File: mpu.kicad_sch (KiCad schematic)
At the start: 15 parts, among them SW401 SW_DIP_x03, U401 STM32MP135FAE7

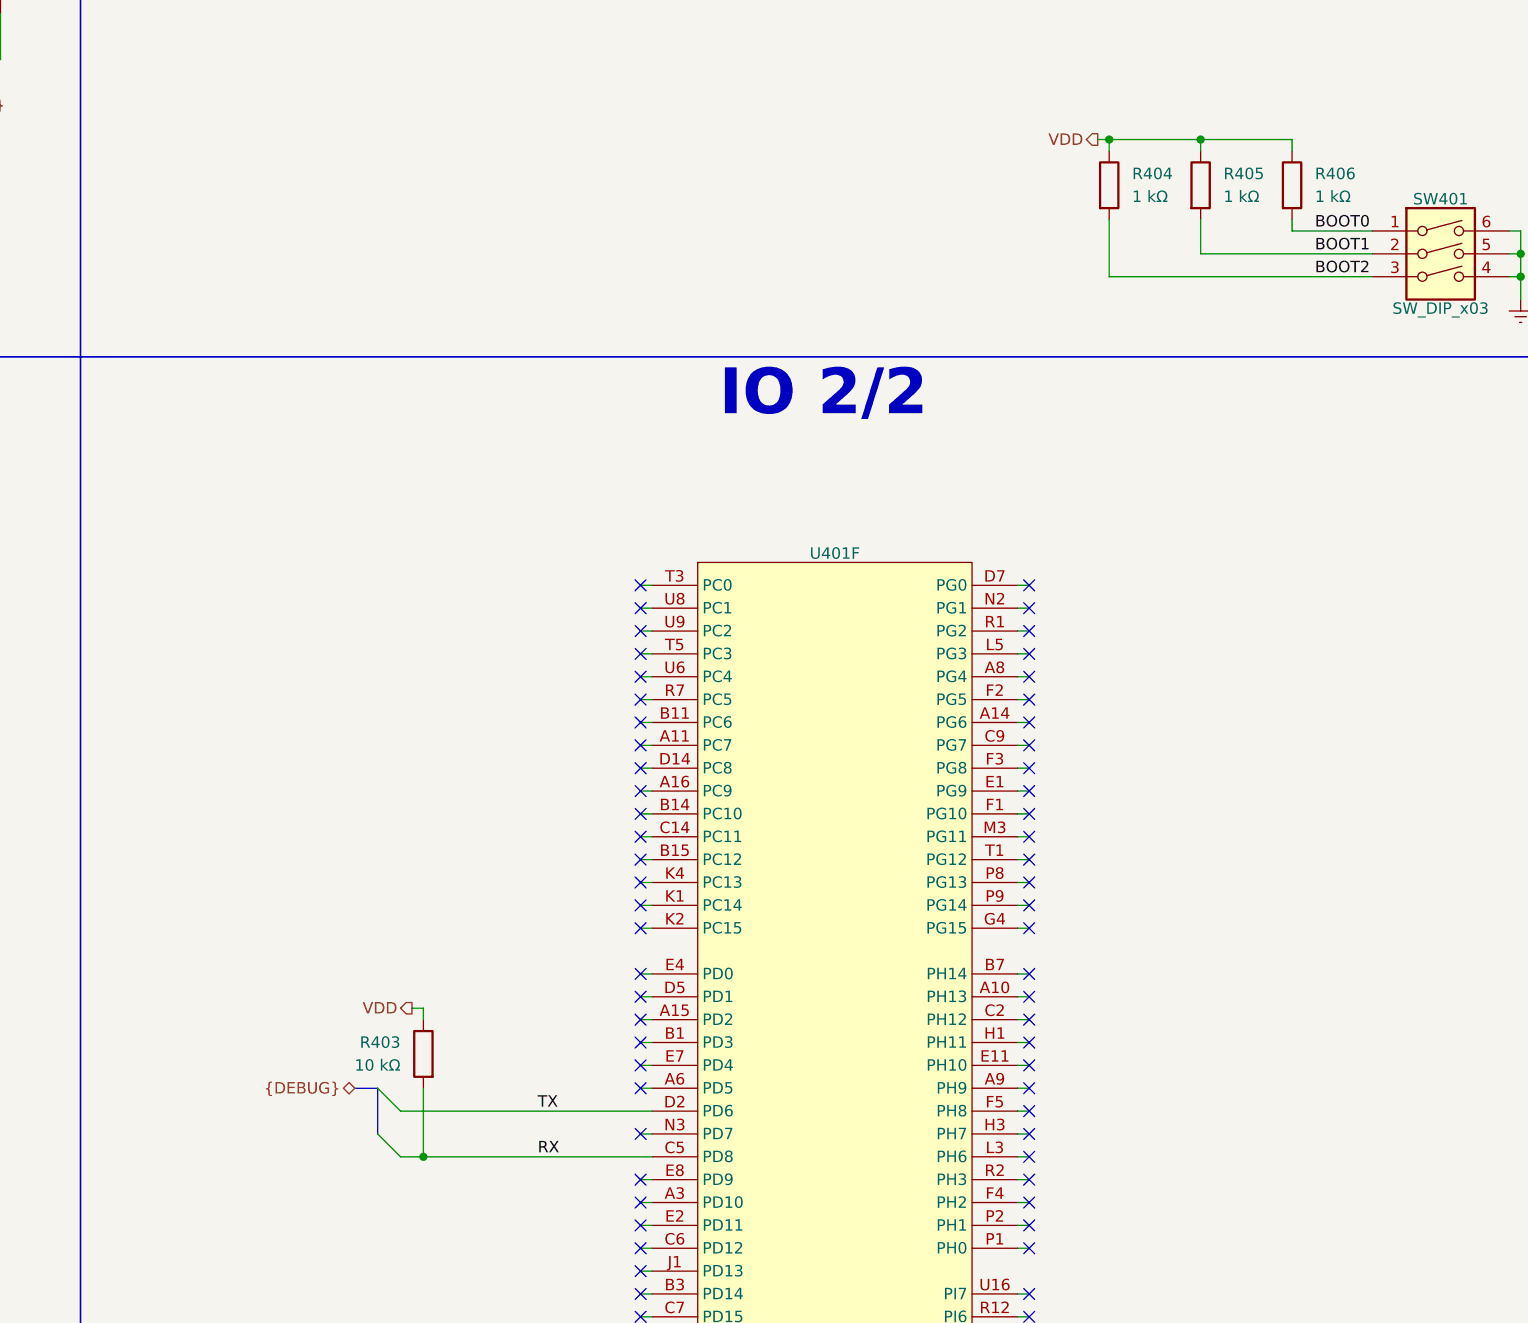
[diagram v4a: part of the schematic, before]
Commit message: Add 10k pull-ups to debug uart
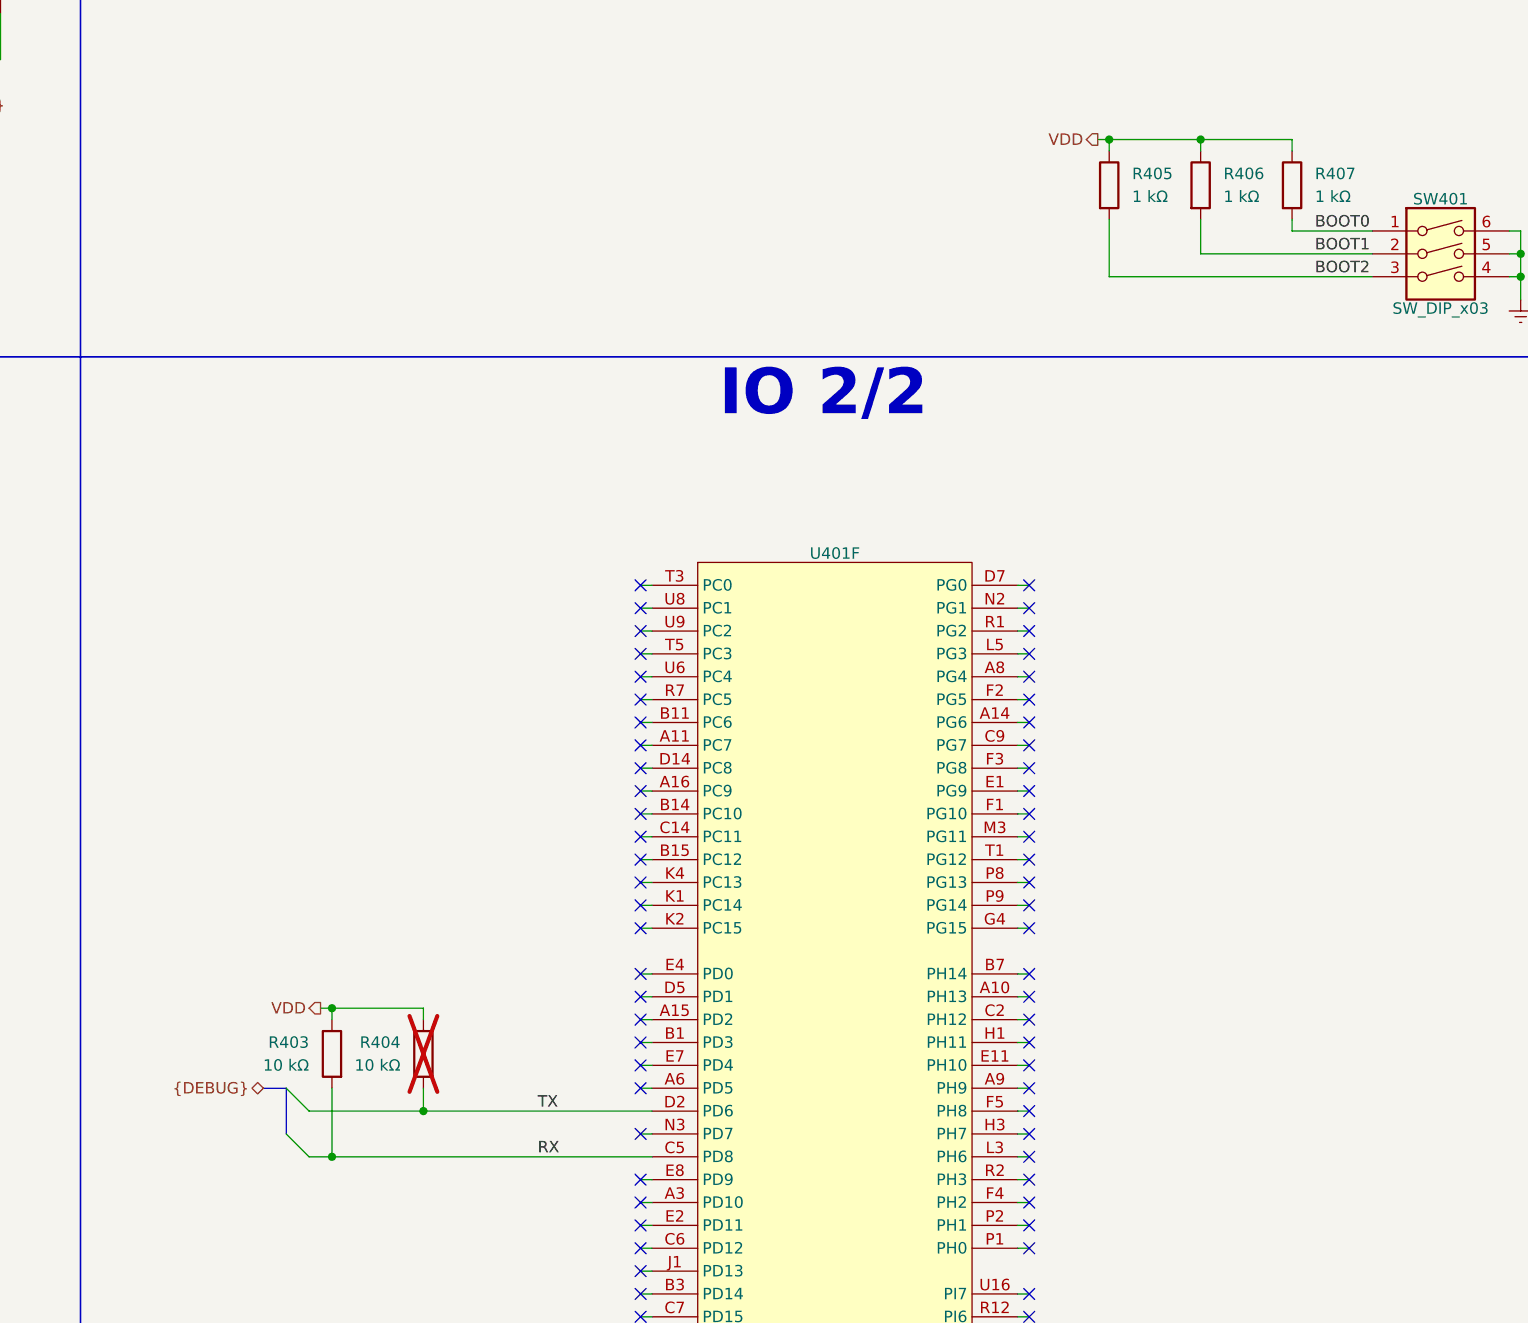
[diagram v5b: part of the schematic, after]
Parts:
- added R404: 10 kΩ, perfect_footprints:R_0402_1005Metric, symbol Device:R
- renumbered R404 to R405, R405 to R406, R406 to R407
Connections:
- net TX: now also R404.2
- net VDD: now also R404.1
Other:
- moved on the sheet: R403
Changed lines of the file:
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@@
 	)
 	(junction
+		(at 279.4 198.12)
+		(diameter 0)
+		(color 0 0 0 0)
+	)
+	(junction
 		(at 83.82 92.71)
 		(diameter 0)
@@
 	)
 	(junction
+		(at 269.24 186.69)
+		(diameter 0)
+		(color 0 0 0 0)
+	)
+	(junction
 		(at 102.87 228.6)
 		(diameter 0)
@@
 	)
 	(junction
-		(at 279.4 203.2)
+		(at 269.24 203.2)
 		(diameter 0)
 		(color 0 0 0 0)
@@
 	)
 	(bus_entry
-		(at 274.32 200.66)
+		(at 264.16 200.66)
 		(size 2.54 2.54)
 		(stroke
@@
 	)
 	(bus_entry
-		(at 274.32 195.58)
+		(at 264.16 195.58)
 		(size 2.54 2.54)
 		(stroke
@@
 	(wire
 		(pts
-			(xy 279.4 186.69) (xy 279.4 187.96)
+			(xy 269.24 186.69) (xy 269.24 187.96)
 		)
 		(stroke
@@
 	(bus
 		(pts
-			(xy 274.32 200.66) (xy 274.32 195.58)
+			(xy 264.16 200.66) (xy 264.16 195.58)
 		)
 		(stroke
@@
 		)
 	)
+	(wire
+		(pts
+			(xy 279.4 195.58) (xy 279.4 198.12)
+		)
+		(stroke
+			(width 0)
+			(type default)
+		)
+	)
 	(bus
 		(pts
@@
 	(wire
 		(pts
-			(xy 279.4 195.58) (xy 279.4 203.2)
+			(xy 269.24 195.58) (xy 269.24 203.2)
 		)
 		(stroke
@@
 	(wire
 		(pts
-			(xy 304.8 203.2) (xy 279.4 203.2)
+			(xy 304.8 203.2) (xy 269.24 203.2)
 		)
 		(stroke
@@
 	(wire
 		(pts
+			(xy 279.4 198.12) (xy 266.7 198.12)
+		)
+		(stroke
+			(width 0)
+			(type default)
+		)
+	)
+	(wire
+		(pts
 			(xy 87.63 154.94) (xy 100.33 154.94)
 		)
@@
 	(wire
 		(pts
-			(xy 279.4 203.2) (xy 276.86 203.2)
+			(xy 269.24 203.2) (xy 266.7 203.2)
 		)
 		(stroke
@@
 	(wire
 		(pts
+			(xy 279.4 187.96) (xy 279.4 186.69)
+		)
+		(stroke
+			(width 0)
+			(type default)
+		)
+	)
+	(wire
+		(pts
 			(xy 163.83 158.75) (xy 162.56 158.75)
 		)
@@
 	(bus
 		(pts
-			(xy 271.78 195.58) (xy 274.32 195.58)
+			(xy 261.62 195.58) (xy 264.16 195.58)
 		)
 		(stroke
@@
 	(wire
 		(pts
-			(xy 278.13 186.69) (xy 279.4 186.69)
+			(xy 267.97 186.69) (xy 269.24 186.69)
 		)
 		(stroke
@@
 		)
 	)
+	(wire
+		(pts
+			(xy 269.24 186.69) (xy 279.4 186.69)
+		)
+		(stroke
+			(width 0)
+			(type default)
+		)
+	)
 	(bus
 		(pts
@@
 	(wire
 		(pts
-			(xy 304.8 198.12) (xy 276.86 198.12)
+			(xy 304.8 198.12) (xy 279.4 198.12)
 		)
 		(stroke
@@
 	(hierarchical_label "{DEBUG}"
 		(shape bidirectional)
-		(at 271.78 195.58 180)
+		(at 261.62 195.58 180)
 		(effects
 			(font
@@
 	(hierarchical_label "VDD"
 		(shape output)
-		(at 278.13 186.69 180)
+		(at 267.97 186.69 180)
 		(effects
 			(font
@@
 		(in_bom yes)
 		(on_board yes)
-		(dnp no)
-		(property "Reference" "R403"
+		(dnp yes)
+		(property "Reference" "R404"
 			(at 276.86 190.4999 0)
 			(effects
@@
 			(project "linux-sbc"
 				(path "/fa11a02f-8043-4153-ab69-88d766503017/2d01087b-54dc-4f43-9cc7-a0ba17201776"
+					(reference "R404")
+					(unit 1)
+				)
+			)
+		)
+	)
+	(symbol
+		(lib_id "Device:R")
+		(at 269.24 191.77 0)
+		(mirror y)
+		(unit 1)
+		(exclude_from_sim no)
+		(in_bom yes)
+		(on_board yes)
+		(dnp no)
+		(property "Reference" "R403"
+			(at 266.7 190.4999 0)
+			(effects
+				(font
+					(size 1.27 1.27)
+				)
+				(justify left)
+			)
+		)
+		(property "Value" "10 kΩ"
+			(at 266.7 193.0399 0)
+			(effects
+				(font
+					(size 1.27 1.27)
+				)
+				(justify left)
+			)
+		)
+		(property "Footprint" "perfect_footprints:R_0402_1005Metric"
+			(at 271.018 191.77 90)
+			(effects
+				(font
+					(size 1.27 1.27)
+				)
+				(hide yes)
+			)
+		)
+		(property "Datasheet" "https://www.we-online.com/components/products/datasheet/560112110020.pdf"
+			(at 269.24 191.77 0)
+			(effects
+				(font
+					(size 1.27 1.27)
+				)
+				(hide yes)
+			)
+		)
+		(property "Description" "Resistor"
+			(at 269.24 191.77 0)
+			(effects
+				(font
+					(size 1.27 1.27)
+				)
+				(hide yes)
+			)
+		)
+		(property "DigiKey Part Number" "732-560112110020CT-ND"
+			(at 269.24 191.77 0)
+			(effects
+				(font
+					(size 1.27 1.27)
+				)
+				(hide yes)
+			)
+		)
+		(property "MPN" "560112110020"
+			(at 269.24 191.77 0)
+			(effects
+				(font
+					(size 1.27 1.27)
+				)
+				(hide yes)
+			)
+		)
+		(property "Manufacturer" "Würth Elektronik"
+			(at 269.24 191.77 0)
+			(effects
+				(font
+					(size 1.27 1.27)
+				)
+				(hide yes)
+			)
+		)
+		(property "Temperature Coefficient" ""
+			(at 269.24 191.77 0)
+			(effects
+				(font
+					(size 1.27 1.27)
+				)
+				(hide yes)
+			)
+		)
+		(pin "2"
+		)
+		(pin "1"
+		)
+		(instances
+			(project "linux-sbc"
+				(path "/fa11a02f-8043-4153-ab69-88d766503017/2d01087b-54dc-4f43-9cc7-a0ba17201776"
 					(reference "R403")
 					(unit 1)
@@
 		(on_board yes)
 		(dnp no)
-		(property "Reference" "R406"
+		(property "Reference" "R407"
 			(at 378.46 93.9799 0)
 			(effects
@@
 			(project "linux-sbc"
 				(path "/fa11a02f-8043-4153-ab69-88d766503017/2d01087b-54dc-4f43-9cc7-a0ba17201776"
-					(reference "R406")
+					(reference "R407")
 					(unit 1)
 				)
@@
 		(on_board yes)
 		(dnp no)
-		(property "Reference" "R404"
+		(property "Reference" "R405"
 			(at 358.14 93.9799 0)
 			(effects
@@
 			(project "linux-sbc"
 				(path "/fa11a02f-8043-4153-ab69-88d766503017/2d01087b-54dc-4f43-9cc7-a0ba17201776"
-					(reference "R404")
+					(reference "R405")
 					(unit 1)
 				)
@@
 		(on_board yes)
 		(dnp no)
-		(property "Reference" "R405"
+		(property "Reference" "R406"
 			(at 368.3 93.9799 0)
 			(effects
@@
 			(project "linux-sbc"
 				(path "/fa11a02f-8043-4153-ab69-88d766503017/2d01087b-54dc-4f43-9cc7-a0ba17201776"
-					(reference "R405")
+					(reference "R406")
 					(unit 1)
 				)

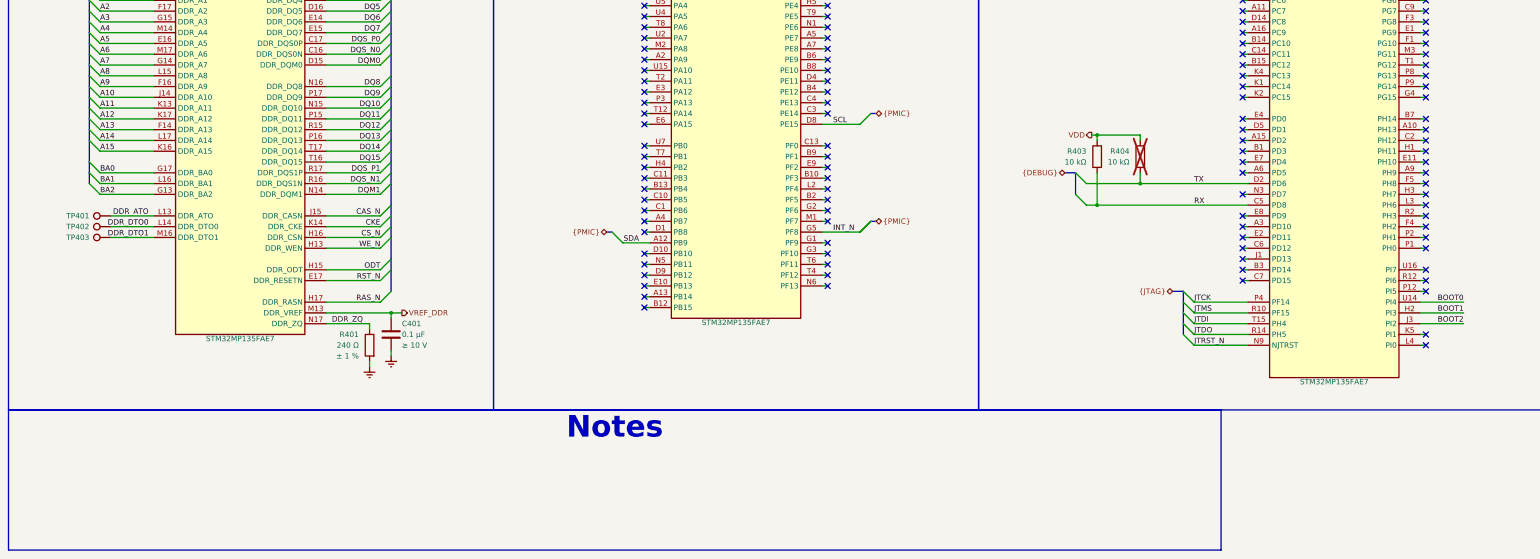
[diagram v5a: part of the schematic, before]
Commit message: Add clocks for MPU
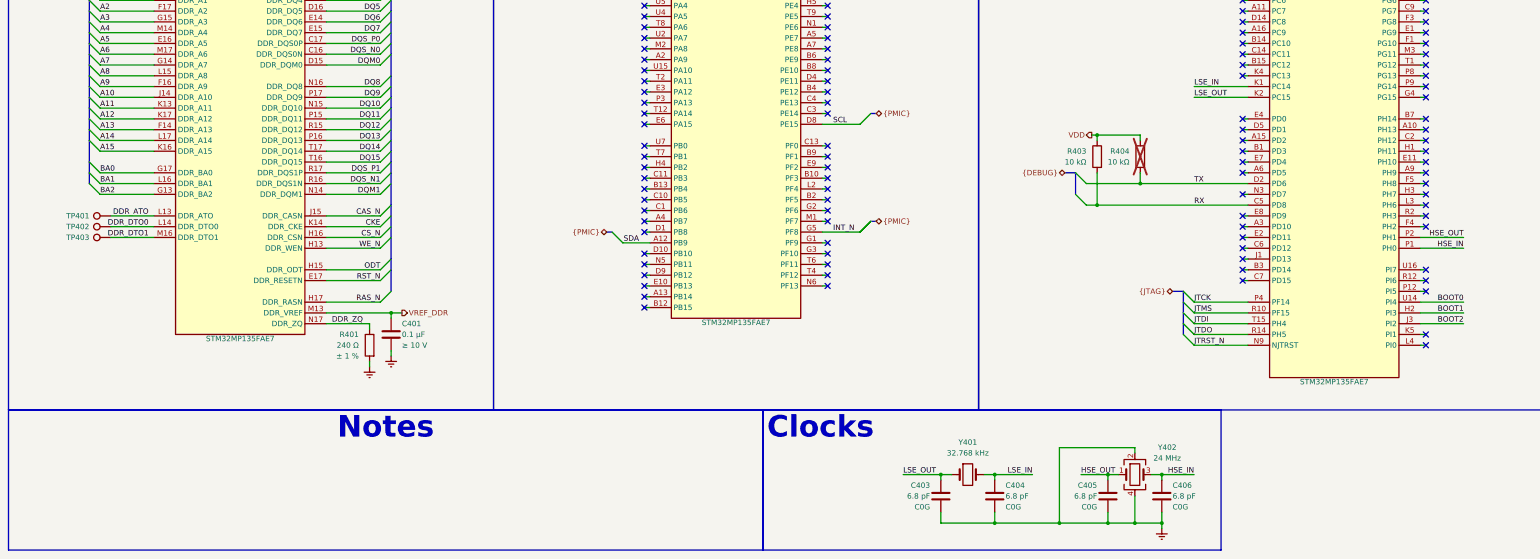
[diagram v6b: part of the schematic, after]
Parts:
- added C403, C404, C405, C406: 6.8 pF, symbol Device:C
- added Y401: 32.768 kHz, symbol Device:Crystal
- added Y402: 24 MHz, MountingHole:MountingHole_2.2mm_M2_DIN965_Pad, symbol Device:Crystal_GND24
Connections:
- net GND: now also C403.2, C404.2, C405.2, C406.2, Y402.2, Y402.4
- net LSE_IN: now reaches U401.K1 (PC14)
- net LSE_IN: now also C404.1, Y401.2
- net LSE_OUT: now reaches U401.K2 (PC15)
- net LSE_OUT: now also C403.1, Y401.1
- net HSE_IN: now reaches U401.P1 (PH0)
- net HSE_IN: now also C406.1, Y402.3
- net HSE_OUT: now reaches U401.P2 (PH1)
- net HSE_OUT: now also C405.1, Y402.1
- no-connect marks 123 -> 119

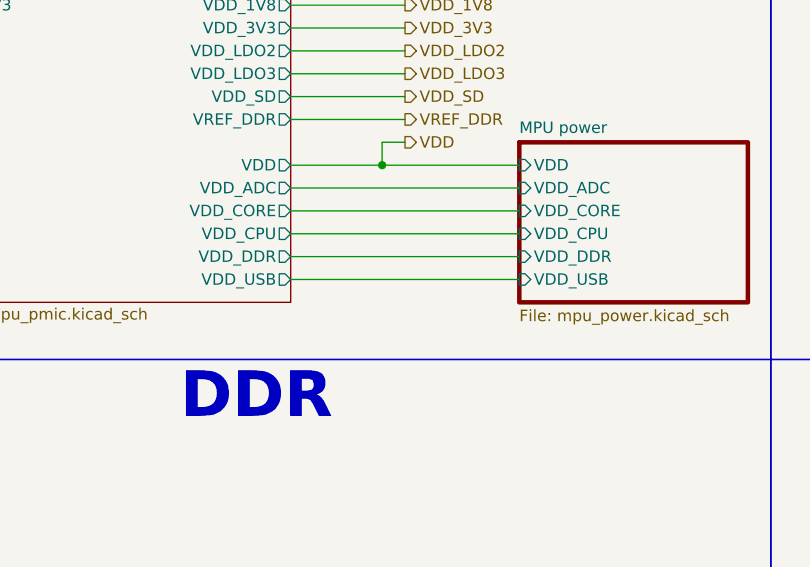
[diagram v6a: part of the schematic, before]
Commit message: Add DDR page
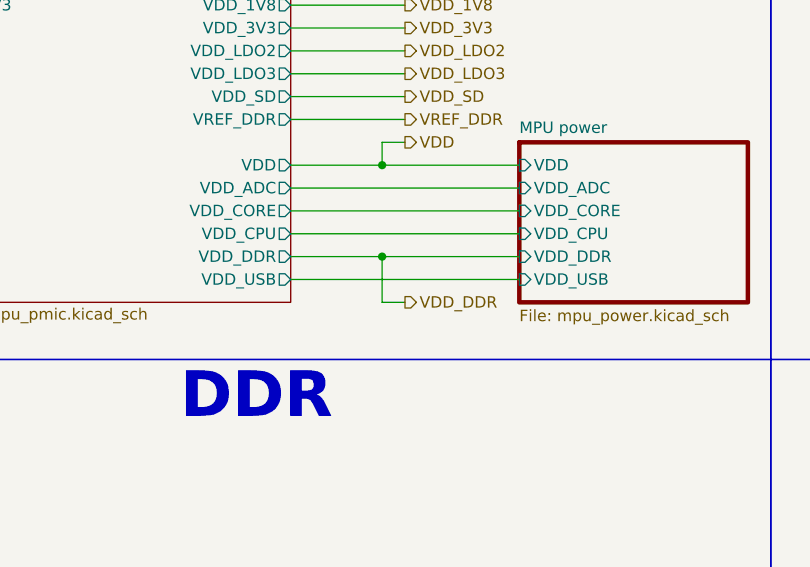
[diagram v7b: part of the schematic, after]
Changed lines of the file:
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@@
 	)
 	(junction
+		(at 83.82 102.87)
+		(diameter 0)
+		(color 0 0 0 0)
+	)
+	(junction
 		(at 365.76 90.17)
 		(diameter 0)
@@
 	(wire
 		(pts
+			(xy 86.36 107.95) (xy 83.82 107.95)
+		)
+		(stroke
+			(width 0)
+			(type default)
+		)
+	)
+	(wire
+		(pts
 			(xy 87.63 185.42) (xy 100.33 185.42)
 		)
@@
 	(wire
 		(pts
-			(xy 73.66 102.87) (xy 99.06 102.87)
+			(xy 73.66 102.87) (xy 83.82 102.87)
 		)
 		(stroke
@@
 		)
 	)
+	(wire
+		(pts
+			(xy 83.82 107.95) (xy 83.82 102.87)
+		)
+		(stroke
+			(width 0)
+			(type default)
+		)
+	)
 	(bus
 		(pts
@@
 		)
 	)
+	(wire
+		(pts
+			(xy 83.82 102.87) (xy 99.06 102.87)
+		)
+		(stroke
+			(width 0)
+			(type default)
+		)
+	)
 	(bus
 		(pts
@@
 		(effects
 			(font
+				(size 1.27 1.27)
+			)
+			(justify left)
+		)
+	)
+	(hierarchical_label "VDD_DDR"
+		(shape output)
+		(at 86.36 107.95 0)
+		(effects
+			(font
